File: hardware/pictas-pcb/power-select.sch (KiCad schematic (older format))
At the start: 1 part, among them U4 TPS2115APWR

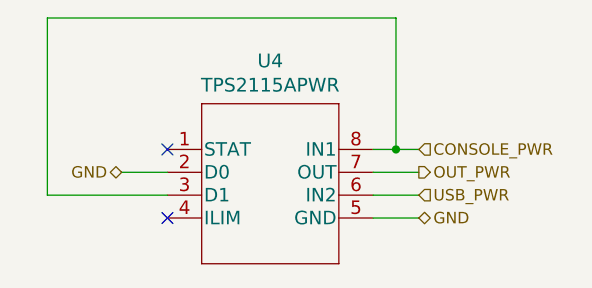
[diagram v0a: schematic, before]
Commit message: Partially working. SPI to FLASH has severe issues on PCB
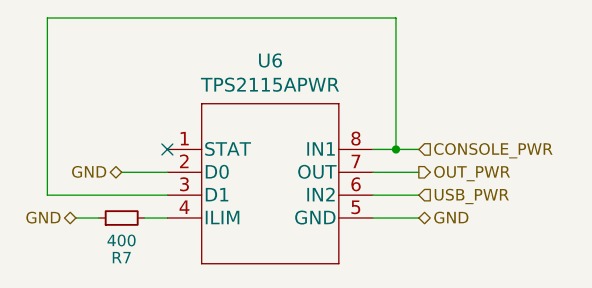
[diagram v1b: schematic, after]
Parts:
- added R7: 400, Resistor_THT:R_Axial_DIN0207_L6.3mm_D2.5mm_P10.16mm_Horizontal, symbol Device:R_Small
- renumbered U4 to U6
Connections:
- net GND: now also R7.1
- net at U6.4 (ILIM): now also R7.2
- no-connect marks 2 -> 1
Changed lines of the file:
@@
 P 5275 3400
 AR Path="/6056FDD3" Ref="U?"  Part="1"
-AR Path="/6056486D/6056FDD3" Ref="U4"  Part="1"
-F 0 "U4" H 5725 3787 60  0000 C CNN
+AR Path="/6056486D/6056FDD3" Ref="U6"  Part="1"
+F 0 "U6" H 5725 3787 60  0000 C CNN
 F 1 "TPS2115APWR" H 5725 3681 60  0000 C CNN
 F 2 "Package_SO:TSSOP-8_4.4x3mm_P0.65mm" H 5725 3640 60  0001 C CNN
@@
 Text HLabel 6375 3400 2    50   Input ~ 0
 CONSOLE_PWR
-NoConn ~ 5275 3700
 NoConn ~ 5275 3400
 Text HLabel 5075 3500 0    50   BiDi ~ 0
@@
 Wire Wire Line
 	6275 3400 6175 3400
+Text HLabel 4875 3700 0    50   BiDi ~ 0
+GND
+$Comp
+L Device:R_Small R7
+U 1 1 61346C51
+P 5075 3700
+F 0 "R7" V 4900 3700 50  0000 C CNN
+F 1 "400" V 4975 3700 50  0000 C CNN
+F 2 "Resistor_THT:R_Axial_DIN0207_L6.3mm_D2.5mm_P10.16mm_Horizontal" H 5075 3700 50  0001 C CNN
+F 3 "~" H 5075 3700 50  0001 C CNN
+	1    5075 3700
+	0    -1   -1   0
+$EndComp
+Wire Wire Line
+	4875 3700 4975 3700
+Wire Wire Line
+	5175 3700 5275 3700
 $EndSCHEMATC
